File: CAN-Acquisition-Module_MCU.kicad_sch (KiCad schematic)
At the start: 32 parts, among them J3 Conn_01x03, J4 Conn_02x05_Odd_Even, U3 M483SGCAE, Y1 12 MHz

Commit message: Layout of analog section started
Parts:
- renumbered C43 to C15, C15 to C16, C45 to C17, C16 to C18, C17 to C19, C18 to C20, C19 to C21, C20 to C22, C21 to C23, C22 to C24, C23 to C25, C24 to C26, C25 to C27, C26 to C28, C27 to C29, C28 to C30, C29 to C31

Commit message: Analog section, screen and USB finished
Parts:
- J3: footprint Connector_PinHeader_1.27mm:PinHeader_1x03_P1.27mm_Vertical -> Connector_PinSocket_2.54mm:PinSocket_1x03_P2.54mm_Vertical
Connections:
- net +3V3: now also J4.1 (Pin_1); no longer J4.2 (Pin_2)
- net GND: now also J4.9 (Pin_9); no longer J4.10 (Pin_10)
- net ICE_CLK: now also J4.5 (Pin_5); no longer J4.6 (Pin_6)
- net ICE_DAT: now also J4.3 (Pin_3); no longer J4.4 (Pin_4)
- net UART0_RX: now also J4.10 (Pin_10); no longer J4.9 (Pin_9)
- net UART0_TX: now also J4.8 (Pin_8); no longer J4.7 (Pin_7)
- net nRESET: now also J4.7 (Pin_7); no longer J4.8 (Pin_8)
- net at U3.8 (PA.11): now also J3.1 (Pin_1); no longer J3.2 (Pin_2)
- net at U3.9 (PA.10): now also J3.2 (Pin_2); no longer J3.1 (Pin_1)
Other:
- moved on the sheet: J3
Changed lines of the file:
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@@
     (stroke (width 0) (type default) (color 0 0 0 0))
   )
-  (wire (pts (xy 132.08 107.95) (xy 132.08 138.43))
+  (wire (pts (xy 132.08 107.95) (xy 132.08 142.24))
     (stroke (width 0) (type default) (color 0 0 0 0))
   )
@@
     (stroke (width 0) (type default) (color 0 0 0 0))
   )
+  (wire (pts (xy 140.97 142.24) (xy 137.16 142.24))
+    (stroke (width 0) (type default) (color 0 0 0 0))
+  )
   (wire (pts (xy 102.87 96.52) (xy 105.41 96.52))
     (stroke (width 0) (type default) (color 0 0 0 0))
@@
     (stroke (width 0) (type default) (color 0 0 0 0))
   )
-  (wire (pts (xy 124.46 138.43) (xy 124.46 137.16))
+  (wire (pts (xy 140.97 142.24) (xy 140.97 153.67))
     (stroke (width 0) (type default) (color 0 0 0 0))
   )
@@
     (stroke (width 0) (type default) (color 0 0 0 0))
   )
-  (wire (pts (xy 124.46 137.16) (xy 129.54 137.16))
-    (stroke (width 0) (type default) (color 0 0 0 0))
-  )
   (wire (pts (xy 27.94 118.11) (xy 27.94 119.38))
     (stroke (width 0) (type default) (color 0 0 0 0))
@@
     (stroke (width 0) (type default) (color 0 0 0 0))
   )
-  (wire (pts (xy 129.54 137.16) (xy 129.54 138.43))
-    (stroke (width 0) (type default) (color 0 0 0 0))
-  )
   (wire (pts (xy 261.62 41.91) (xy 270.51 41.91))
     (stroke (width 0) (type default) (color 0 0 0 0))
@@
     (stroke (width 0) (type default) (color 0 0 0 0))
   )
-  (wire (pts (xy 134.62 107.95) (xy 134.62 138.43))
+  (wire (pts (xy 134.62 107.95) (xy 134.62 142.24))
     (stroke (width 0) (type default) (color 0 0 0 0))
   )
@@
     (effects (font (size 3 3)) (justify left bottom))
   )
-  (text "UART6_RXD" (at 135.89 156.21 90)
+  (text "UART6_RXD" (at 135.89 160.02 90)
     (effects (font (size 1.27 1.27)) (justify left bottom))
   )
@@
     (effects (font (size 1.27 1.27)) (justify left bottom))
   )
-  (text "UART6_TXD" (at 133.35 156.21 90)
+  (text "UART6_TXD" (at 133.35 160.02 90)
     (effects (font (size 1.27 1.27)) (justify left bottom))
   )
@@
     (pin "2")
   )
-  (symbol (lib_id "Connector_Generic:Conn_02x05_Odd_Even") (at 245.11 34.29 0) (unit 1)
+  (symbol (lib_id "Connector_Generic:Conn_02x05_Odd_Even") (at 247.65 34.29 0) (mirror y) (unit 1)
     (in_bom yes) (on_board yes)
     (property "Reference" "J4" (id 0) (at 246.38 26.67 0))
-    (property "Value" "Conn_02x05_Odd_Even" (id 1) (at 245.11 41.91 0))
-    (property "Footprint" "Connector_PinSocket_2.54mm:PinSocket_2x05_P2.54mm_Vertical" (id 2) (at 245.11 34.29 0)
-      (effects (font (size 1.27 1.27)) hide)
-    )
-    (property "Datasheet" "~" (id 3) (at 245.11 34.29 0)
+    (property "Value" "Conn_02x05_Odd_Even" (id 1) (at 247.65 41.91 0))
+    (property "Footprint" "Connector_PinSocket_2.54mm:PinSocket_2x05_P2.54mm_Vertical" (id 2) (at 247.65 34.29 0)
+      (effects (font (size 1.27 1.27)) hide)
+    )
+    (property "Datasheet" "~" (id 3) (at 247.65 34.29 0)
       (effects (font (size 1.27 1.27)) hide)
     )
@@
     (pin "2")
   )
-  (symbol (lib_id "power:GND") (at 124.46 138.43 0) (unit 1)
-    (in_bom yes) (on_board yes)
-    (property "Reference" "#PWR054" (id 0) (at 124.46 144.78 0)
-      (effects (font (size 1.27 1.27)) hide)
-    )
-    (property "Value" "GND" (id 1) (at 124.587 142.8242 0))
-    (property "Footprint" "" (id 2) (at 124.46 138.43 0)
-      (effects (font (size 1.27 1.27)) hide)
-    )
-    (property "Datasheet" "" (id 3) (at 124.46 138.43 0)
+  (symbol (lib_id "power:GND") (at 140.97 153.67 0) (unit 1)
+    (in_bom yes) (on_board yes)
+    (property "Reference" "#PWR054" (id 0) (at 140.97 160.02 0)
+      (effects (font (size 1.27 1.27)) hide)
+    )
+    (property "Value" "GND" (id 1) (at 141.097 158.0642 0))
+    (property "Footprint" "" (id 2) (at 140.97 153.67 0)
+      (effects (font (size 1.27 1.27)) hide)
+    )
+    (property "Datasheet" "" (id 3) (at 140.97 153.67 0)
       (effects (font (size 1.27 1.27)) hide)
     )
@@
     (pin "1")
   )
-  (symbol (lib_id "Connector_Generic:Conn_01x03") (at 132.08 143.51 270) (unit 1)
+  (symbol (lib_id "Connector_Generic:Conn_01x03") (at 134.62 147.32 90) (mirror x) (unit 1)
     (in_bom yes) (on_board yes) (fields_autoplaced)
-    (property "Reference" "J3" (id 0) (at 136.652 142.6753 90)
-      (effects (font (size 1.27 1.27)) (justify left))
-    )
-    (property "Value" "Conn_01x03" (id 1) (at 136.652 145.2122 90)
-      (effects (font (size 1.27 1.27)) (justify left))
-    )
-    (property "Footprint" "Connector_PinHeader_1.27mm:PinHeader_1x03_P1.27mm_Vertical" (id 2) (at 132.08 143.51 0)
-      (effects (font (size 1.27 1.27)) hide)
-    )
-    (property "Datasheet" "~" (id 3) (at 132.08 143.51 0)
-      (effects (font (size 1.27 1.27)) hide)
-    )
+    (property "Reference" "J3" (id 0) (at 139.192 146.4853 90)
+      (effects (font (size 1.27 1.27)) (justify right))
+    )
+    (property "Value" "Conn_01x03" (id 1) (at 139.192 149.0222 90)
+      (effects (font (size 1.27 1.27)) (justify right))
+    )
+    (property "Footprint" "Connector_PinSocket_2.54mm:PinSocket_1x03_P2.54mm_Vertical" (id 2) (at 134.62 147.32 0)
+      (effects (font (size 1.27 1.27)) hide)
+    )
+    (property "Datasheet" "~" (id 3) (at 134.62 147.32 0)
+      (effects (font (size 1.27 1.27)) hide)
+    )

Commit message: Finished power outputs
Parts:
- added D8, D9: CM1213A-01SO, Package_TO_SOT_SMD:SOT-23, symbol Power_Protection:CM1213A-01SO
- added R13: Ω, Resistor_SMD:R_0603_1608Metric, symbol Device:R_Small_US
- J4: footprint Connector_PinSocket_2.54mm:PinSocket_2x05_P2.54mm_Vertical -> CAN-Acquisition-Module:Nu-Link-Me-v3.0
- renumbered C15 to C14, C16 to C15, C17 to C16, C18 to C17, C19 to C18, C20 to C19, C21 to C20, C22 to C21, C23 to C22, C24 to C23, C25 to C24, C26 to C25, C27 to C26, C28 to C27, C29 to C28, C30 to C29, C31 to C30, R13 to R14
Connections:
- net +3V3: now also D8.2 (VP), D9.2 (VP), R13.2; no longer J4.1 (Pin_1)
- net GND: now also J4.1 (Pin_1), D8.3 (VN), D9.3 (VN); no longer J4.9 (Pin_9)
- net ICE_DAT: now also J4.7 (Pin_7); no longer J4.3 (Pin_3)
- net UART0_RX: now also J4.2 (Pin_2); no longer J4.10 (Pin_10)
- net UART0_TX: now also J4.4 (Pin_4); no longer J4.8 (Pin_8)
- net nRESET: now also J4.3 (Pin_3); no longer J4.7 (Pin_7)
- net at J3.1 (Pin_1), U3.8 (PA.11): now also D8.1 (CH1)
- net at J3.2 (Pin_2), U3.9 (PA.10): now also D9.1 (CH1)
- new net: J4.9 (Pin_9), R13.1
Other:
- moved on the sheet: C30, J4, R14

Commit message: forgor to save
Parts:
- renumbered C14 to C15, C15 to C16, C16 to C17, C17 to C18, C18 to C19, C19 to C20, C20 to C21, C21 to C22, C22 to C23, C23 to C24, C24 to C25, C25 to C26, C26 to C27, C27 to C28, C28 to C29, C29 to C30, C30 to C31

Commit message: Rev. A1 release
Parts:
- added C32: 100 nF, Capacitor_SMD:C_0402_1005Metric, symbol Device:C_Small
- added R13, R14: 10 kΩ, Resistor_SMD:R_0603_1608Metric, symbol Device:R_Small_US
- added U4: SST25VF080B-50-4x-S2Ax, CAN-Acquisition-Module:SOIC-8_P1.27mm_Multi, symbol Memory_Flash:SST25VF080B-50-4x-S2Ax
- renumbered R13 to R15, R14 to R16
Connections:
- net +3V3: now also C32.1, R13.1, R14.1, U4.8 (VDD)
- net GND: now also C32.2, U4.4 (VSS)
- net MEM_MISO: now reaches U3.18 (PC.7)
- net MEM_MISO: now also U4.2 (SO)
- net MEM_MOSI: now reaches U3.19 (PC.6)
- net MEM_MOSI: now also U4.5 (SI)
- net MEM_CLK: now reaches U3.20 (PA.7)
- net MEM_CLK: now also U4.6 (SCK)
- net MEM_nSS: now reaches U3.21 (PA.6)
- net MEM_nSS: now also U4.1 (~{CE})
- new net: R14.2, U4.3 (~{WP})
- new net: R13.2, U4.7 (~{HOLD})
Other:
- note added: "SPI1_CLK"
- note added: "SPI1_MISO"
- note added: "SPI1_MOSI"
- note added: "SPI1_SS"
- note removed: "SPI bus for external memory chip could go here"
- note removed: "}"

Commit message: Added as-ordered P/Ns and regenerated Gerbers
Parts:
- C27, C30: Mfr. (none) -> Stackpole; P/N (none) -> CML0603C0G200JT50V
- D7: Mfr. (none) -> Wurth Electronics; P/N (none) -> 150141M173100
- D8, D9: Mfr. (none) -> Diodes Incorporated; P/N (none) -> D1213A-01SO-7
- L4, L5: Mfr. (none) -> Eaton; P/N (none) -> MFBM1V1608-300-R
- R10: Mfr. (none) -> Panasonic; P/N (none) -> ERJ-3EKF3000V
- R11, R12: Mfr. (none) -> Stackpole; P/N (none) -> RMCF0603FT120R
- R13, R14, R16: Mfr. (none) -> Stackpole; P/N (none) -> RMCF0603FT10K0
- U3: Mfr. (none) -> Nuvoton; P/N (none) -> M483SGCAE
- Y1: Mfr. (none) -> Aker Technology; P/N (none) -> C3E-12.000-18-3030-X-R
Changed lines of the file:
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@@
+      (effects (font (size 1.27 1.27)) hide)
+    )
+    (property "Mfr." "Nuvoton" (id 4) (at 107.95 54.61 0)
+      (effects (font (size 1.27 1.27)) hide)
+    )
+    (property "P/N" "M483SGCAE" (id 5) (at 107.95 54.61 0)
       (effects (font (size 1.27 1.27)) hide)
     )
@@
       (effects (font (size 1.27 1.27)) hide)
     )
+    (property "Mfr." "Stackpole" (id 4) (at 270.51 45.72 0)
+      (effects (font (size 1.27 1.27)) hide)
+    )
+    (property "P/N" "RMCF0603FT10K0" (id 5) (at 270.51 45.72 0)
+      (effects (font (size 1.27 1.27)) hide)
+    )
     (pin "1")
     (pin "2")
@@
     )
     (property "Datasheet" "~" (id 3) (at 182.88 106.68 0)
+      (effects (font (size 1.27 1.27)) hide)
+    )
+    (property "Mfr." "Aker Technology" (id 4) (at 182.88 106.68 0)
+      (effects (font (size 1.27 1.27)) hide)
+    )
+    (property "P/N" "C3E-12.000-18-3030-X-R" (id 5) (at 182.88 106.68 0)
       (effects (font (size 1.27 1.27)) hide)
     )
@@
       (effects (font (size 1.27 1.27)) hide)
     )
+    (property "Mfr." "Stackpole" (id 4) (at 193.04 102.87 0)
+      (effects (font (size 1.27 1.27)) hide)
+    )
+    (property "P/N" "CML0603C0G200JT50V" (id 5) (at 193.04 102.87 0)
+      (effects (font (size 1.27 1.27)) hide)
+    )
     (pin "1")
     (pin "2")
@@
     )
     (property "Datasheet" "~" (id 3) (at 171.45 110.49 0)
+      (effects (font (size 1.27 1.27)) hide)
+    )
+    (property "Mfr." "Stackpole" (id 4) (at 171.45 110.49 0)
+      (effects (font (size 1.27 1.27)) hide)
+    )
+    (property "P/N" "CML0603C0G200JT50V" (id 5) (at 171.45 110.49 0)
       (effects (font (size 1.27 1.27)) hide)
     )
@@
       (effects (font (size 1.27 1.27)) hide)
     )
+    (property "Mfr." "Eaton" (id 4) (at 34.29 149.86 0)
+      (effects (font (size 1.27 1.27)) hide)
+    )
+    (property "P/N" "MFBM1V1608-300-R" (id 5) (at 34.29 149.86 0)
+      (effects (font (size 1.27 1.27)) hide)
+    )
     (pin "1")
     (pin "2")
@@
       (effects (font (size 1.27 1.27)) hide)
     )
+    (property "Mfr." "Eaton" (id 4) (at 34.29 139.7 0)
+      (effects (font (size 1.27 1.27)) hide)
+    )
+    (property "P/N" "MFBM1V1608-300-R" (id 5) (at 34.29 139.7 0)
+      (effects (font (size 1.27 1.27)) hide)
+    )
     (pin "1")
     (pin "2")
@@
       (effects (font (size 1.27 1.27)) hide)
     )
+    (property "Mfr." "Stackpole" (id 4) (at 55.88 71.12 0)
+      (effects (font (size 1.27 1.27)) hide)
+    )
+    (property "P/N" "RMCF0603FT120R" (id 5) (at 55.88 71.12 0)
+      (effects (font (size 1.27 1.27)) hide)
+    )
     (pin "1")
     (pin "2")
@@
       (effects (font (size 1.27 1.27)) hide)
     )
+    (property "Mfr." "Diodes Incorporated" (id 4) (at 113.03 152.4 0)
+      (effects (font (size 1.27 1.27)) hide)
+    )
+    (property "P/N" "D1213A-01SO-7" (id 5) (at 113.03 152.4 0)
+      (effects (font (size 1.27 1.27)) hide)
+    )
     (pin "1")
     (pin "2")
@@
     )
     (property "Datasheet" "~" (id 3) (at 208.28 140.97 0)
+      (effects (font (size 1.27 1.27)) hide)
+    )
+    (property "Mfr." "Stackpole" (id 4) (at 208.28 140.97 0)
+      (effects (font (size 1.27 1.27)) hide)
+    )
+    (property "P/N" "RMCF0603FT10K0" (id 5) (at 208.28 140.97 0)
       (effects (font (size 1.27 1.27)) hide)
     )
@@
       (effects (font (size 1.27 1.27)) hide)
     )
+    (property "Mfr." "Stackpole" (id 4) (at 55.88 76.2 0)
+      (effects (font (size 1.27 1.27)) hide)
+    )
+    (property "P/N" "RMCF0603FT120R" (id 5) (at 55.88 76.2 0)
+      (effects (font (size 1.27 1.27)) hide)
+    )
     (pin "1")
     (pin "2")
@@
     )
     (property "Datasheet" "http://www.onsemi.com/pub_link/Collateral/CM1213A-D.PDF" (id 3) (at 126.492 150.495 90)
+      (effects (font (size 1.27 1.27)) hide)
+    )
+    (property "Mfr." "Diodes Incorporated" (id 4) (at 124.46 152.4 0)
+      (effects (font (size 1.27 1.27)) hide)
+    )
+    (property "P/N" "D1213A-01SO-7" (id 5) (at 124.46 152.4 0)
       (effects (font (size 1.27 1.27)) hide)
     )
@@
       (effects (font (size 1.27 1.27)) hide)
     )
+    (property "Mfr." "Wurth Electronics" (id 4) (at 43.18 71.12 0)
+      (effects (font (size 1.27 1.27)) hide)
+    )
+    (property "P/N" "150141M173100" (id 5) (at 43.18 71.12 0)
+      (effects (font (size 1.27 1.27)) hide)
+    )
     (pin "1")
     (pin "2")
@@
       (effects (font (size 1.27 1.27)) hide)
     )
+    (property "Mfr." "Stackpole" (id 4) (at 199.39 140.97 0)
+      (effects (font (size 1.27 1.27)) hide)
+    )
+    (property "P/N" "RMCF0603FT10K0" (id 5) (at 199.39 140.97 0)
+      (effects (font (size 1.27 1.27)) hide)
+    )
     (pin "1")
     (pin "2")
@@
       (effects (font (size 1.27 1.27)) hide)
     )
+    (property "Mfr." "Panasonic" (id 4) (at 55.88 66.04 0)
+      (effects (font (size 1.27 1.27)) hide)
+    )
+    (property "P/N" "ERJ-3EKF3000V" (id 5) (at 55.88 66.04 0)
+      (effects (font (size 1.27 1.27)) hide)
+    )

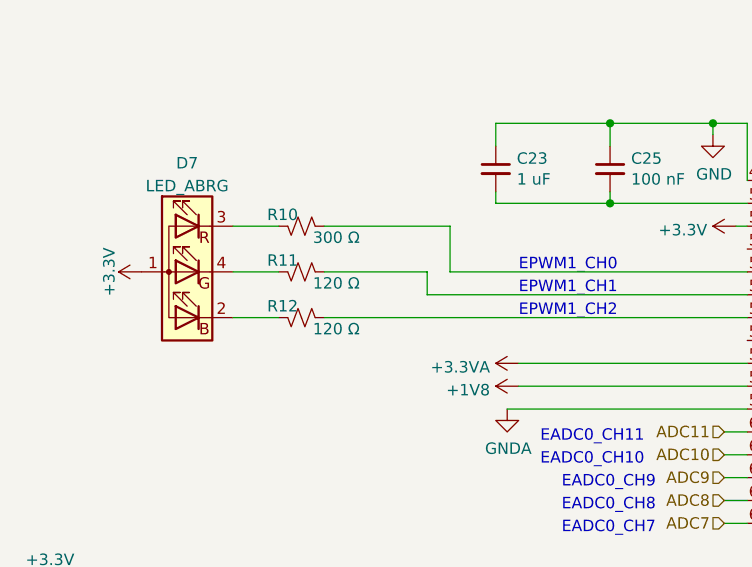
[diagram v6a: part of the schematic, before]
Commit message: Rev. A2
U1 had wrong pinout. NT1 label removed from silk. Green LED resistor increased in value
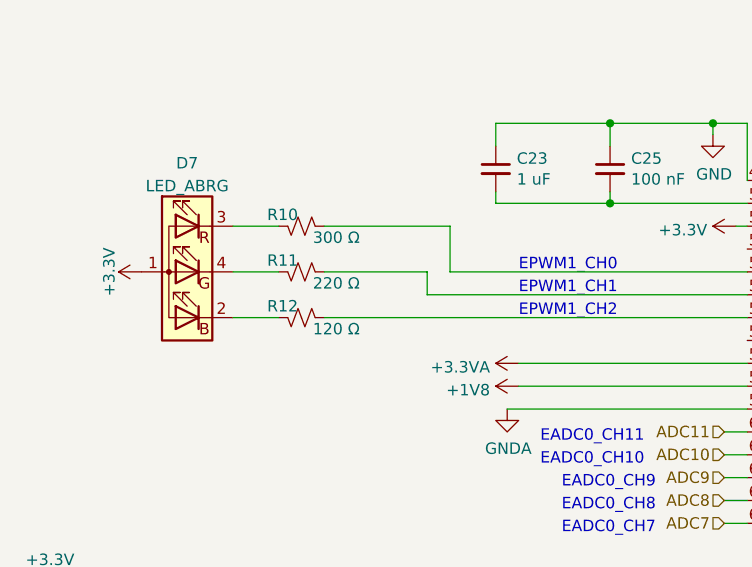
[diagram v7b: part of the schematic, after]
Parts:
- R11: value 120 Ω -> 220 Ω
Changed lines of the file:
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@@
     (title "CANbus Acquisition Module")
     (date "2022-06-01")
-    (rev "A1")
+    (rev "A2")
     (company "École de Technologie Supérieure - Laboratoire thermique et science du bâtiment (LTSB)")
     (comment 1 "Designer: Hugo Boyce")
@@
       (effects (font (size 1.27 1.27)) (justify left))
     )
-    (property "Value" "120 Ω" (id 1) (at 57.15 72.39 90)
-      (effects (font (size 1.27 1.27)) (justify left))
-    )
+    (property "Value" "220 Ω" (id 1) (at 57.15 72.39 90)
+      (effects (font (size 1.27 1.27)) (justify left))
+    )
